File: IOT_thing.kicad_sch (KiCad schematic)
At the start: 54 parts, among them J1 USB_C_Receptacle_USB2.0_16P, J2 Conn_01x04, J3 Screw_Terminal_01x03, J4 Screw_Terminal_01x08, J5 Screw_Terminal_01x02, K1 RT314A05, Q1 UMH3N, Q2 UMH3N, Q3 BC817, SW1 SW_SPST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

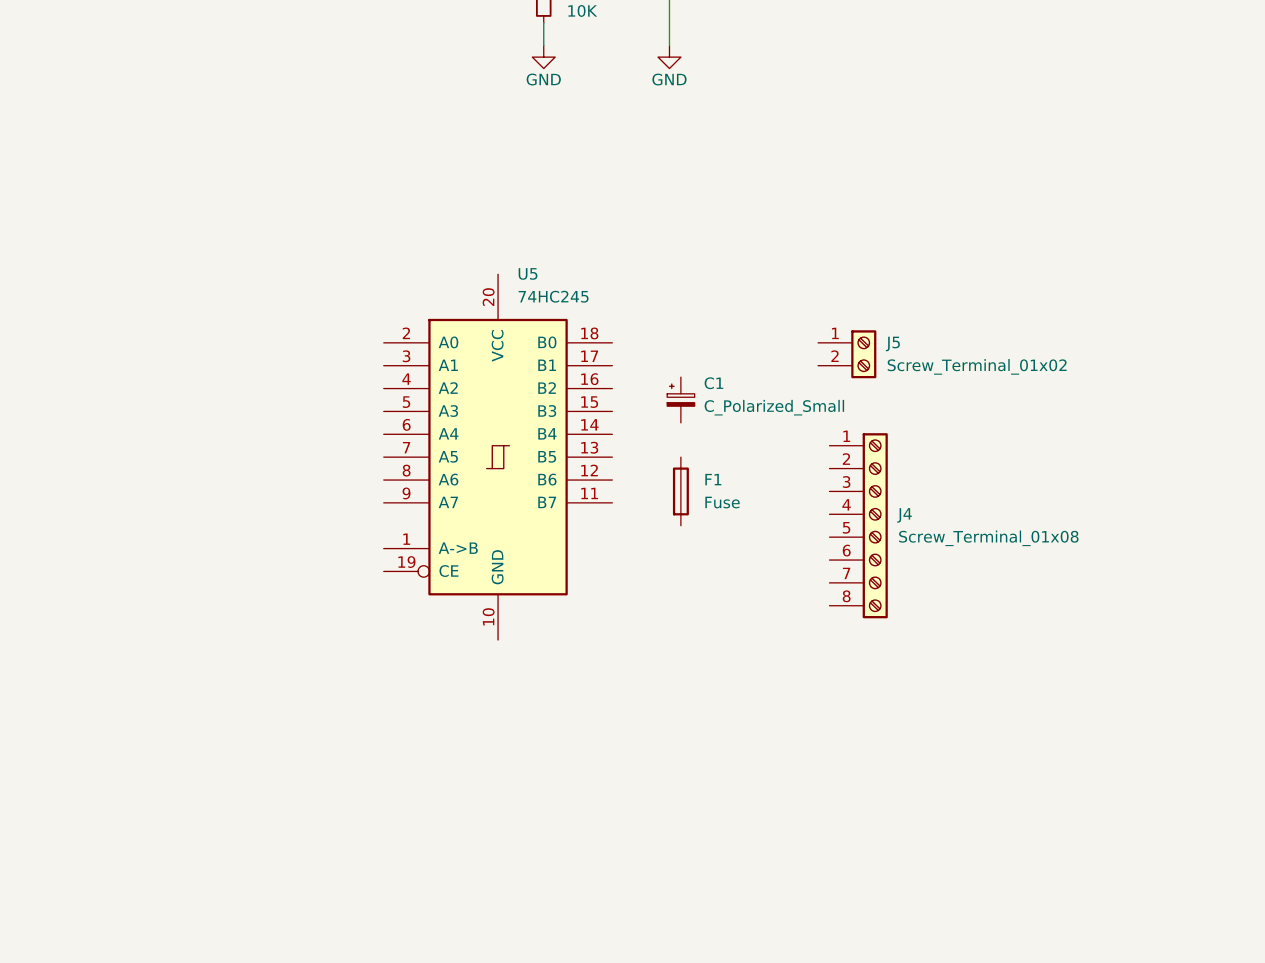
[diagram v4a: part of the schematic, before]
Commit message: Finished wiring the ledstrip part
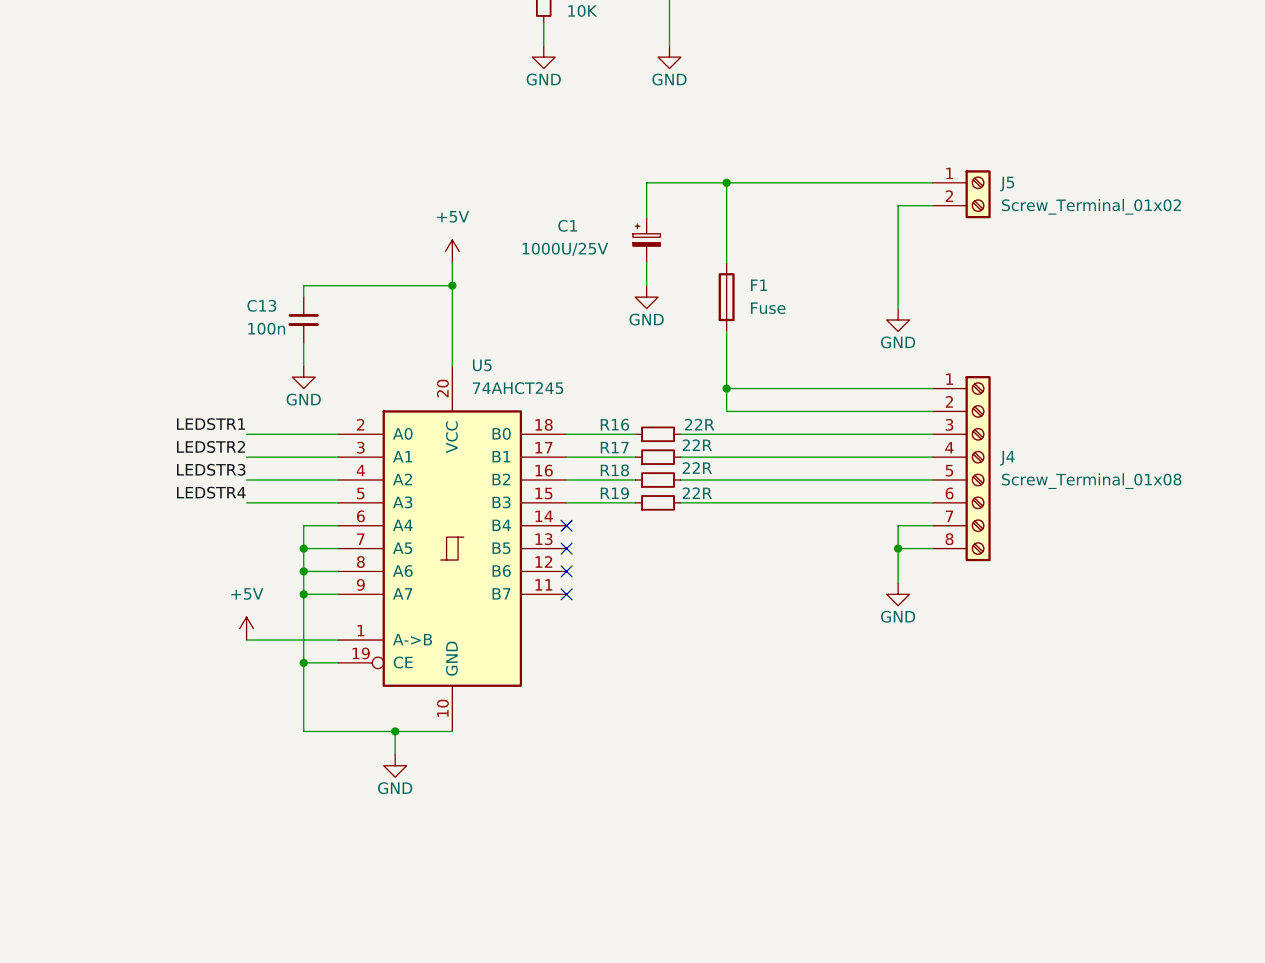
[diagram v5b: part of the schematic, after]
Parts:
- added C13: 100n, symbol Device:C_Small
- added R16, R17, R18, R19: 22R, symbol Device:R_Small
- C1: value C_Polarized_Small -> 1000U/25V
- U5: value 74HC245 -> 74AHCT245
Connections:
- net +5V: now also U5.1 (A->B), U5.20 (VCC), C13.1
- net GND: now also C1.2, J4.7 (Pin_7), J4.8 (Pin_8), J5.2 (Pin_2), U5.10 (GND), U5.19 (CE), U5.6 (A4), U5.7 (A5), U5.8 (A6), U5.9 (A7), C13.2
- net at F1.1: now also C1.1, J5.1 (Pin_1)
- net at F1.2: now also J4.1 (Pin_1), J4.2 (Pin_2)
- net at J4.3 (Pin_3): now also R16.2
- net at J4.4 (Pin_4): now also R17.2
- net at J4.5 (Pin_5): now also R18.2
- net at J4.6 (Pin_6): now also R19.2
- net at U5.15 (B3): now also R19.1
- net at U5.16 (B2): now also R18.1
- net at U5.17 (B1): now also R17.1
- net at U5.18 (B0): now also R16.1
- net LEDSTR1: now reaches U5.2 (A0)
- net LEDSTR2: now reaches U5.3 (A1)
- net LEDSTR3: now reaches U5.4 (A2)
- net LEDSTR4: now reaches U5.5 (A3)
- no-connect marks 0 -> 4
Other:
- moved on the sheet: C1, F1, J4, J5, U5

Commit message: Completed commenting on the sheet and did annotations
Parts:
- added C10: 22u, symbol Device:C_Small
- added C14, C15: 100n, symbol Device:C_Small
- added J6: Conn_02x05_Odd_Even, symbol Connector_Generic:Conn_02x05_Odd_Even
- added R20: 1K, symbol Device:R_Small
- renumbered Ce to Ce1
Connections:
- net EN is gone; now on net +3.3V: Q2.1 (E1)
- net RED_B is gone; now on net LED_B: R10.1
- net RED_G is gone; now on net LED_G: R9.1
- net RED_R is gone; now on net LED_R: R7.1
- net +3.3V: now also U1.2 (VDD), U1.3 (EN), C10.1, C14.1, J6.1 (Pin_1), J6.2 (Pin_2), R20.1
- net GND: now also U1.1 (GND), U1.15 (GND), U1.38 (GND), U1.39 (GND), C10.2, C14.2, C15.2, J6.10 (Pin_10), J6.9 (Pin_9)
- net IO0: now also U1.25 (IO0)
- net LEDSTR1: now also U1.27 (IO16)
- net LEDSTR2: now also U1.28 (IO17)
- net LEDSTR3: now also U1.30 (IO18)
- net LEDSTR4: now also U1.31 (IO19)
- net RELAY: now also U1.10 (IO25)
- net RX: now also U1.35 (TXD0/IO1)
- net SCL: now also U1.37 (IO23)
- net SDA: now also U1.36 (IO22)
- net SW: now also U1.33 (IO21)
- net TX: now also U1.34 (RXD0/IO3)
- net GPIO26: now reaches U1.11 (IO26)
- net GPIO26: now also J6.3 (Pin_3)
- net GPIO27: now reaches U1.12 (IO27)
- net GPIO27: now also J6.5 (Pin_5)
- net LED_B: now reaches U1.13 (IO14)
- net LED_R: now reaches U1.16 (IO13)
- net LED_G: now reaches U1.23 (IO15)
- net GPIO34: now reaches U1.6 (IO34)
- net GPIO34: now also J6.6 (Pin_6)
- net GPIO35: now reaches U1.7 (IO35)
- net GPIO35: now also J6.8 (Pin_8)
- net GPIO32: now reaches U1.8 (IO32)
- net GPIO32: now also J6.7 (Pin_7)
- net GPIO33: now reaches U1.9 (IO33)
- net GPIO33: now also J6.4 (Pin_4)
- new net: C15.1, R20.2
- no-connect marks 4 -> 9
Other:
- note added: "I2C - QWIIC CONNECTOR"
- note added: "LDO 5V TO 3.3V"
- note added: "LED DRIVER"
- note added: "MCU"
- note added: "MOUNTING"
- note added: "POWER + PROGRAMMING UNIT"
- note added: "RELAY"
- note added: "USER I/O"
- moved on the sheet: C7, C8, C9, D1, D2, D3, D4, H1, H2, H3, H4, J3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

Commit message: Completed adding footprints
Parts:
- C1, C10, C11, C2, C5, C7, C8: footprint (none) -> Capacitor_THT:CP_Radial_D10.0mm_P5.00mm
- C12, C13, C14, C15, C4, C6, C9: footprint (none) -> Capacitor_SMD:C_0402_1005Metric_Pad0.74x0.62mm_HandSolder
- C3, Ce1: footprint (none) -> Capacitor_SMD:C_0805_2012Metric_Pad1.18x1.45mm_HandSolder
- D2, D4: footprint (none) -> LED_SMD:LED_0603_1608Metric_Pad1.05x0.95mm_HandSolder
- D3: footprint (none) -> LED_SMD:LED_RGB_Wuerth-PLCC4_3.2x2.8mm_150141M173100
- F1: footprint (none) -> Fuse:FUSE_696105003002
- F2: footprint (none) -> Fuse:Fuse_1206_3216Metric_Pad1.42x1.75mm_HandSolder
- FB1: footprint (none) -> Inductor_SMD:L_0603_1608Metric_Pad1.05x0.95mm_HandSolder
- H1, H2, H3, H4: footprint (none) -> MountingHole:MountingHole_3.2mm_M3_Pad_Via
- J1: footprint (none) -> Connector_USB:USB_C_Receptacle_HRO_TYPE-C-31-M-12
- J2: footprint (none) -> Connector_JST:JST_SH_SM04B-SRSS-TB_1x04-1MP_P1.00mm_Horizontal
- J3: footprint (none) -> TerminalBlock_Phoenix:TerminalBlock_Phoenix_MKDS-3-3-5.08_1x03_P5.08mm_Horizontal
- J4: footprint (none) -> TerminalBlock_Phoenix:TerminalBlock_Phoenix_MKDS-1,5-8_1x08_P5.00mm_Horizontal
- J5: footprint (none) -> TerminalBlock_Phoenix:TerminalBlock_Phoenix_MKDS-1,5-2-5.08_1x02_P5.08mm_Horizontal
- J6: footprint (none) -> Connector_PinHeader_2.54mm:PinHeader_2x05_P2.54mm_Vertical_SMD
- R1, R10, R11, R12, R13, R14, R15, R16, R17, R18, R19, R2, R20, R3, R4, R5, R6, R7, R8, R9: footprint (none) -> Resistor_SMD:R_0402_1005Metric_Pad0.72x0.64mm_HandSolder
- SW1: footprint (none) -> Button_Switch_SMD1:SW_Push_1P1T_NO_6x6mm_H9.5mm
- U5: footprint (none) -> Package_DIP:DIP-22_W7.62mm
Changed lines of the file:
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@@
 			)
 		)
-		(property "Footprint" ""
+		(property "Footprint" "Capacitor_THT:CP_Radial_D10.0mm_P5.00mm"
 			(at 76.2 152.4 0)
 			(effects
@@
 			)
 		)
-		(property "Footprint" ""
+		(property "Footprint" "TerminalBlock_Phoenix:TerminalBlock_Phoenix_MKDS-3-3-5.08_1x03_P5.08mm_Horizontal"
 			(at 373.38 133.35 0)
 			(effects
@@
 			)
 		)
-		(property "Footprint" ""
+		(property "Footprint" "Fuse:FUSE_696105003002"
 			(at 337.312 194.31 90)
 			(effects
@@
 			)
 		)
-		(property "Footprint" ""
+		(property "Footprint" "Resistor_SMD:R_0402_1005Metric_Pad0.72x0.64mm_HandSolder"
 			(at 331.47 212.09 0)
 			(effects
@@
 			)
 		)
-		(property "Footprint" ""
+		(property "Footprint" "Capacitor_SMD:C_0402_1005Metric_Pad0.74x0.62mm_HandSolder"
 			(at 292.1 196.85 0)
 			(effects
@@
 			)
 		)
-		(property "Footprint" ""
+		(property "Footprint" "TerminalBlock_Phoenix:TerminalBlock_Phoenix_MKDS-1,5-2-5.08_1x02_P5.08mm_Horizontal"
 			(at 367.03 181.61 0)
 			(effects
@@
 			)
 		)
-		(property "Footprint" ""
+		(property "Footprint" "Resistor_SMD:R_0402_1005Metric_Pad0.72x0.64mm_HandSolder"
 			(at 71.12 81.28 0)
 			(effects
@@
 			)
 		)
-		(property "Footprint" ""
+		(property "Footprint" "Resistor_SMD:R_0402_1005Metric_Pad0.72x0.64mm_HandSolder"
 			(at 81.28 81.28 0)
 			(effects
@@
 			)
 		)
-		(property "Footprint" ""
+		(property "Footprint" "Resistor_SMD:R_0402_1005Metric_Pad0.72x0.64mm_HandSolder"
 			(at 304.8 39.37 0)
 			(effects
@@
 			)
 		)
-		(property "Footprint" ""
+		(property "Footprint" "Resistor_SMD:R_0402_1005Metric_Pad0.72x0.64mm_HandSolder"
 			(at 316.23 39.37 0)
 			(effects
@@
 			)
 		)
-		(property "Footprint" ""
+		(property "Footprint" "LED_SMD:LED_0603_1608Metric_Pad1.05x0.95mm_HandSolder"
 			(at 99.06 152.4 0)
 			(effects
@@
 			)
 		)
-		(property "Footprint" ""
+		(property "Footprint" "Capacitor_SMD:C_0402_1005Metric_Pad0.74x0.62mm_HandSolder"
 			(at 66.04 217.17 0)
 			(effects
@@
 			)
 		)
-		(property "Footprint" ""
+		(property "Footprint" "Capacitor_THT:CP_Radial_D10.0mm_P5.00mm"
 			(at 40.64 152.4 0)
 			(effects
@@
 			)
 		)
-		(property "Footprint" ""
+		(property "Footprint" "LED_SMD:LED_0603_1608Metric_Pad1.05x0.95mm_HandSolder"
 			(at 297.18 130.81 0)
 			(effects
@@
 			)
 		)
-		(property "Footprint" ""
+		(property "Footprint" "MountingHole:MountingHole_3.2mm_M3_Pad_Via"
 			(at 101.6 259.08 0)
 			(effects
@@
 			)
 		)
-		(property "Footprint" ""
+		(property "Footprint" "Resistor_SMD:R_0402_1005Metric_Pad0.72x0.64mm_HandSolder"
 			(at 191.77 46.99 0)
 			(effects
@@
 			)
 		)
-		(property "Footprint" ""
+		(property "Footprint" "Capacitor_THT:CP_Radial_D10.0mm_P5.00mm"
 			(at 330.2 187.96 0)
 			(effects
@@
 			)
 		)
-		(property "Footprint" ""
+		(property "Footprint" "Connector_USB:USB_C_Receptacle_HRO_TYPE-C-31-M-12"
 			(at 45.72 69.85 0)
 			(effects
@@
 			)
 		)
-		(property "Footprint" ""
+		(property "Footprint" "Capacitor_SMD:C_0805_2012Metric_Pad1.18x1.45mm_HandSolder"
 			(at 132.08 43.18 0)
 			(effects
@@
 			)
 		)
-		(property "Footprint" ""
+		(property "Footprint" "Resistor_SMD:R_0402_1005Metric_Pad0.72x0.64mm_HandSolder"
 			(at 331.47 209.55 0)
 			(effects
@@
 			)
 		)
-		(property "Footprint" ""
+		(property "Footprint" "TerminalBlock_Phoenix:TerminalBlock_Phoenix_MKDS-1,5-8_1x08_P5.00mm_Horizontal"
 			(at 367.03 212.09 0)
 			(effects
@@
 			)
 		)
-		(property "Footprint" ""
+		(property "Footprint" "Resistor_SMD:R_0402_1005Metric_Pad0.72x0.64mm_HandSolder"
 			(at 312.42 153.67 0)
 			(effects
@@
 			)
 		)
-		(property "Footprint" ""
+		(property "Footprint" "MountingHole:MountingHole_3.2mm_M3_Pad_Via"
 			(at 82.55 259.08 0)
 			(effects
@@
 			)
 		)
-		(property "Footprint" ""
+		(property "Footprint" "Capacitor_THT:CP_Radial_D10.0mm_P5.00mm"
 			(at 331.47 33.02 0)
 			(effects
@@
 			)
 		)
-		(property "Footprint" ""
+		(property "Footprint" "Inductor_SMD:L_0603_1608Metric_Pad1.05x0.95mm_HandSolder"
 			(at 72.39 36.322 90)
 			(effects
@@
 			)
 		)
-		(property "Footprint" ""
+		(property "Footprint" "Resistor_SMD:R_0402_1005Metric_Pad0.72x0.64mm_HandSolder"
 			(at 331.47 214.63 0)
 			(effects
@@
 			)
 		)
-		(property "Footprint" ""
+		(property "Footprint" "Capacitor_SMD:C_0402_1005Metric_Pad0.74x0.62mm_HandSolder"
 			(at 195.58 139.7 0)
 			(effects
@@
 			)
 		)
-		(property "Footprint" ""
+		(property "Footprint" "Capacitor_SMD:C_0402_1005Metric_Pad0.74x0.62mm_HandSolder"
 			(at 193.04 33.02 0)
 			(effects
@@
 			)
 		)
-		(property "Footprint" ""
+		(property "Footprint" "Capacitor_SMD:C_0402_1005Metric_Pad0.74x0.62mm_HandSolder"
 			(at 115.57 43.18 0)
 			(effects
@@
 			)
 		)
-		(property "Footprint" ""
+		(property "Footprint" "Button_Switch_SMD1:SW_Push_1P1T_NO_6x6mm_H9.5mm"
 			(at 50.8 213.36 0)
 			(effects
@@
 			)
 		)
-		(property "Footprint" ""
+		(property "Footprint" "Capacitor_THT:CP_Radial_D10.0mm_P5.00mm"
 			(at 181.61 33.02 0)
 			(effects
@@
 			)
 		)
-		(property "Footprint" ""
+		(property "Footprint" "MountingHole:MountingHole_3.2mm_M3_Pad_Via"
 			(at 63.5 259.08 0)
 			(effects
@@
 			)
 		)
-		(property "Footprint" ""
+		(property "Footprint" "Resistor_SMD:R_0402_1005Metric_Pad0.72x0.64mm_HandSolder"
 			(at 144.78 43.18 0)
 			(effects
@@
 			)
 		)
-		(property "Footprint" ""
+		(property "Footprint" "Resistor_SMD:R_0402_1005Metric_Pad0.72x0.64mm_HandSolder"
 			(at 331.47 217.17 0)
 			(effects
@@
 			)
 		)
-		(property "Footprint" ""
+		(property "Footprint" "Capacitor_SMD:C_0805_2012Metric_Pad1.18x1.45mm_HandSolder"
 			(at 139.7 95.25 0)
 			(effects
@@
 			)
 		)
-		(property "Footprint" ""
+		(property "Footprint" "Resistor_SMD:R_0402_1005Metric_Pad0.72x0.64mm_HandSolder"
 			(at 297.18 121.92 0)
 			(effects
@@
 			)
 		)
-		(property "Footprint" ""
+		(property "Footprint" "Resistor_SMD:R_0402_1005Metric_Pad0.72x0.64mm_HandSolder"
 			(at 167.64 160.02 0)
 			(effects
@@
 			)
 		)
-		(property "Footprint" ""
+		(property "Footprint" "Resistor_SMD:R_0402_1005Metric_Pad0.72x0.64mm_HandSolder"
 			(at 66.04 207.01 0)
 			(effects
@@
 			)
 		)
-		(property "Footprint" ""
+		(property "Footprint" "Resistor_SMD:R_0402_1005Metric_Pad0.72x0.64mm_HandSolder"
 			(at 109.22 209.55 0)
 			(effects
@@
 			)
 		)
-		(property "Footprint" ""
+		(property "Footprint" "Fuse:Fuse_1206_3216Metric_Pad1.42x1.75mm_HandSolder"
 			(at 92.71 36.83 0)
 			(effects
@@
 			)
 		)
-		(property "Footprint" ""
+		(property "Footprint" "Capacitor_THT:CP_Radial_D10.0mm_P5.00mm"
 			(at 184.15 139.7 0)
 			(effects
@@
 			)
 		)
-		(property "Footprint" ""
+		(property "Footprint" "Resistor_SMD:R_0402_1005Metric_Pad0.72x0.64mm_HandSolder"
 			(at 109.22 214.63 0)
 			(effects
@@
 			)
 		)
-		(property "Footprint" ""
+		(property "Footprint" "Capacitor_SMD:C_0402_1005Metric_Pad0.74x0.62mm_HandSolder"
 			(at 347.98 67.31 0)
 			(effects
@@
 			)
 		)
-		(property "Footprint" ""
+		(property "Footprint" "Resistor_SMD:R_0402_1005Metric_Pad0.72x0.64mm_HandSolder"
 			(at 300.99 147.32 0)
 			(effects
@@
 			)
 		)
-		(property "Footprint" ""
+		(property "Footprint" "Capacitor_THT:CP_Radial_D10.0mm_P5.00mm"
 			(at 104.14 43.18 0)
 			(effects
@@
 			)
 		)
-		(property "Footprint" ""
+		(property "Footprint" "Package_DIP:DIP-22_W7.62mm"
 			(at 308.61 222.25 0)
 			(effects
@@
 			)
 		)
-		(property "Footprint" ""
+		(property "Footprint" "MountingHole:MountingHole_3.2mm_M3_Pad_Via"
 			(at 44.45 259.08 0)
 			(effects
@@
 			)
 		)
-		(property "Footprint" ""
+		(property "Footprint" "Connector_PinHeader_2.54mm:PinHeader_2x05_P2.54mm_Vertical_SMD"
 			(at 163.83 262.89 0)
 			(effects
@@
 			)
 		)
-		(property "Footprint" ""
+		(property "Footprint" "Capacitor_SMD:C_0402_1005Metric_Pad0.74x0.62mm_HandSolder"
 			(at 167.64 168.91 0)
 			(effects
@@
 			)
 		)
-		(property "Footprint" ""
+		(property "Footprint" "Connector_JST:JST_SH_SM04B-SRSS-TB_1x04-1MP_P1.00mm_Horizontal"
 			(at 364.49 44.45 0)
 			(effects
@@
 			)
 		)
-		(property "Footprint" ""
+		(property "Footprint" "Resistor_SMD:R_0402_1005Metric_Pad0.72x0.64mm_HandSolder"
 			(at 109.22 219.71 0)
 			(effects
@@
 			)
 		)
-		(property "Footprint" ""
+		(property "Footprint" "Resistor_SMD:R_0402_1005Metric_Pad0.72x0.64mm_HandSolder"
 			(at 191.77 49.53 0)
 			(effects
@@
 			)
 		)
-		(property "Footprint" ""
+		(property "Footprint" "LED_SMD:LED_RGB_Wuerth-PLCC4_3.2x2.8mm_150141M173100"
 			(at 121.92 215.9 0)
 			(effects
@@
 			)
 		)
-		(property "Footprint" ""
+		(property "Footprint" "Resistor_SMD:R_0402_1005Metric_Pad0.72x0.64mm_HandSolder"
 			(at 99.06 144.78 0)
 			(effects
